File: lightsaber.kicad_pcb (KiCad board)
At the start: 2 copper layers, 31 x 112.5 mm, 8 parts, among them SW1 Button, SW3 POWER, U1 C3 Pico

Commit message: Update PCB for Lightsaber
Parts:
- removed SW3: POWER, as12ap:as12ap
- added SW2: POWER, Button_Switch_SMD:SW_SPDT_CK_JS102011SAQN, B.Cu at (110.7, 59.9)
- added TP1: TO-BAT, TestPoint:TestPoint_Loop_D2.50mm_Drill1.0mm, F.Cu at (113.1, 48.6)
- R1, R2, SW1: moved to B.Cu
- moved R2 124.6 mm to (106.5, 159.1), turned to 180 degrees
- moved R1 52.6 mm to (114.0, 158.7), turned to 0 degrees
- moved R3 48.1 mm to (111.5, 157.5), turned to 90 degrees
- moved BT1 36.3 mm to (120.8, 57.9)
- moved U1 33.9 mm to (120.5, 147.5)
- moved NP1 24.8 mm to (120.5, 39.0)
- moved SW1 22.2 mm to (128.9, 56.0), turned to -90 degrees
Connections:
- BT1 pad 1: +4V -> VBAT
- U1 pad 15: +4V -> unconnected-(U1-IO3/VBAT-Pad15)
- U1 pad 16: Power -> unconnected-(U1-RST/EN-Pad16)
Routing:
- net GND: track 112.6 -> 0.00 mm, vias 4 -> 0
- net +3V3: track 110.2 -> 2.65 mm
- net +4V: track 115.4 -> 24.5 mm
- net Poti: track 103.5 -> 12.8 mm
- net Light: track 33.8 -> 6.13 mm
- net Power: track 23.0 -> 0.00 mm
- net Button: track 84.8 -> 100.0 mm
- net Neopixel: track 101.9 -> 116.5 mm
- net VBAT: track 0.00 -> 8.12 mm
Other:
- board size 31 x 112.5 mm -> 31.5 x 126 mm

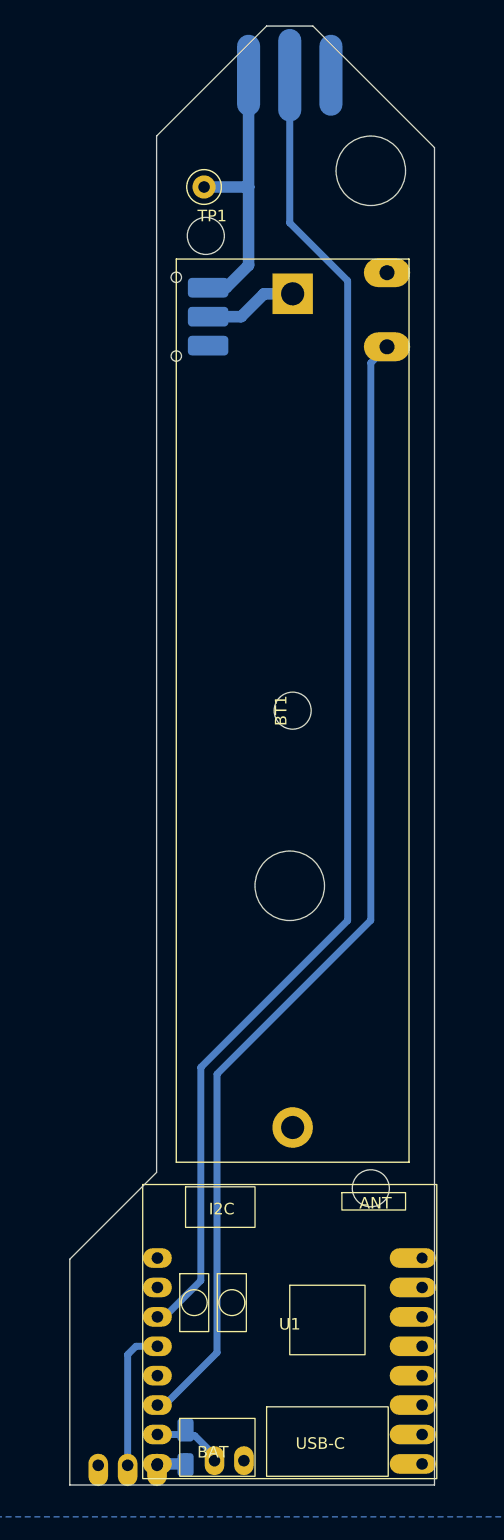
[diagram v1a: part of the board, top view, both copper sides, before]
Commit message: Fixed switch between 5V and V_Batt
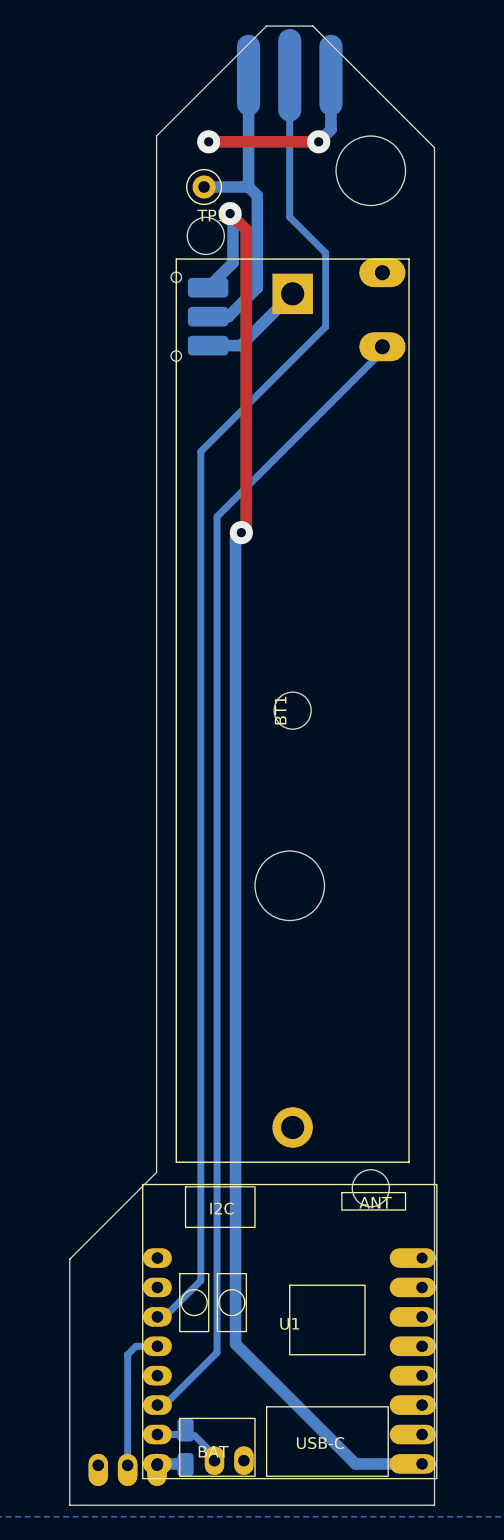
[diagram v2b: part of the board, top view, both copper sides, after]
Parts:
- R3: value R -> 100k
- moved SW1 0.40 mm to (128.5, 56.0)
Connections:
- SW2 pad 1: unconnected-(SW2-A-Pad1) -> VBAT
- SW2 pad 2: VBAT -> +4V
- SW2 pad 3: +4V -> +5V
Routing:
- net +5V: track 0.00 -> 126.4 mm, vias 0 -> 2
- net GND: track 0.00 -> 15.7 mm, vias 0 -> 2
- net +4V: track 24.5 -> 27.8 mm
- net Neopixel: track 116.5 -> 114.9 mm
- net VBAT: track 8.12 -> 9.15 mm
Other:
- board size 31.5 x 126 mm -> 31.5 x 127.8 mm
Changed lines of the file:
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@@
 		(pad_to_mask_clearance 0)
 		(allow_soldermask_bridges_in_footprints no)
-		(grid_origin 120.5 39)
+		(grid_origin 120.5 35)
 		(pcbplotparams
 			(layerselection 0x0001000_fffffffe)
@@
 	(net 17 "unconnected-(U1-IO3{slash}VBAT-Pad15)")
 	(net 18 "VBAT")
-	(net 19 "unconnected-(SW2-A-Pad1)")
 	(footprint "c3-pico:c3-pico"
 		(layer "F.Cu")
@@
 		(model "${KIPRJMOD}/lib/c3-pico/c3-pico.step"
 			(offset
+				(xyz 0 0 2.54)
+			)
+			(scale
+				(xyz 1 1 1)
+			)
+			(rotate
 				(xyz 0 0 0)
+			)
+		)
+		(model "${KICAD_3DMODEL_DIR}/Connector_PinHeader_2.54mm.3dshapes/PinHeader_1x08_P2.54mm_Vertical.wrl"
+			(offset
+				(xyz -11.5 6.5 0)
+			)
+			(scale
+				(xyz 1 1 1)
+			)
+			(rotate
+				(xyz 0 0 0)
+			)
+		)
+		(model "${KICAD_3DMODEL_DIR}/Connector_PinHeader_2.54mm.3dshapes/PinHeader_1x08_P2.54mm_Vertical.wrl"
+			(offset
+				(xyz 11.5 6.5 0)
 			)
 			(scale
@@
 			)
 		)
-		(property "Value" "R"
+		(property "Value" "100k"
 			(at 0 -1.65 90)
 			(layer "B.Fab")
@@
 			(layers "B.Cu" "B.Paste" "B.Mask")
 			(roundrect_rratio 0.2)
-			(net 19 "unconnected-(SW2-A-Pad1)")
+			(net 18 "VBAT")
 			(pinfunction "A")
-			(pintype "passive+no_connect")
+			(pintype "passive")
 		)
 		(pad "2" smd roundrect
@@
 			(layers "B.Cu" "B.Paste" "B.Mask")
 			(roundrect_rratio 0.2)
-			(net 18 "VBAT")
+			(net 3 "+4V")
 			(pinfunction "B")
 			(pintype "passive")
@@
 			(layers "B.Cu" "B.Paste" "B.Mask")
 			(roundrect_rratio 0.2)
-			(net 3 "+4V")
+			(net 13 "+5V")
 			(pinfunction "C")
 			(pintype "passive")
@@
 	(footprint "pts636:pts636"
 		(layer "B.Cu")
-		(at 128.9 56.05 -90)
+		(at 128.5 56.05 -90)
 		(descr "<b>PTS636 SM43 LFS-1</b><br>")
 		(property "Reference" "SW1"
@@
 	(gr_poly
 		(pts
-			(xy 133 160.75) (xy 101.5 160.75) (xy 101.5 141.25) (xy 109 133.75) (xy 109 44.25) (xy 118.5 34.75)
+			(xy 133 162.5) (xy 101.5 162.5) (xy 101.5 141.25) (xy 109 133.75) (xy 109 44.25) (xy 118.5 34.75)
 			(xy 122.5 34.75) (xy 133 45.25)
 		)
@@
 	)
 	(segment
-		(start 113.45 57.35)
-		(end 115 57.35)
+		(start 123 44.75)
+		(end 113.5 44.75)
+		(width 1)
+		(layer "F.Cu")
+		(net 1)
+	)
+	(via
+		(at 113.5 44.75)
+		(size 2)
+		(drill 0.8)
+		(layers "F.Cu" "B.Cu")
+		(net 1)
+	)
+	(via
+		(at 123 44.75)
+		(size 2)
+		(drill 0.8)
+		(layers "F.Cu" "B.Cu")
+		(net 1)
+	)
+	(segment
+		(start 124.056 43.694)
+		(end 123 44.75)
+		(width 1)
+		(layer "B.Cu")
+		(net 1)
+	)
+	(segment
+		(start 124.056 39)
+		(end 124.056 43.694)
+		(width 1)
+		(layer "B.Cu")
+		(net 1)
+	)
+	(segment
+		(start 113.45 59.85)
+		(end 115.2 59.85)
 		(width 1)
 		(layer "B.Cu")
@@
 	)
 	(segment
-		(start 116.944 55.406)
+		(start 115.2 59.85)
+		(end 117.7 57.35)
+		(width 1)
+		(layer "B.Cu")
+		(net 3)
+	)
+	(segment
+		(start 117.7 49.406)
 		(end 116.944 48.65)
 		(width 1)
@@
 	)
 	(segment
-		(start 115 57.35)
-		(end 116.944 55.406)
+		(start 117.7 57.35)
+		(end 117.7 49.406)
 		(width 1)
 		(layer "B.Cu")
@@
 	)
 	(segment
-		(start 125.5 56.75)
-		(end 120.5 51.75)
-		(width 0.6)
-		(layer "B.Cu")
-		(net 5)
-	)
-	(segment
-		(start 120.5 51.75)
-		(end 120.5 39)
-		(width 0.6)
-		(layer "B.Cu")
-		(net 5)
-	)
-	(segment
-		(start 125.5 112)
-		(end 125.5 56.75)
-		(width 0.6)
-		(layer "B.Cu")
-		(net 5)
-	)
-	(segment
-		(start 112.82 143.097716)
-		(end 112.82 124.68)
-		(width 0.6)
-		(layer "B.Cu")
-		(net 5)
-	)
-	(segment
 		(start 109.687716 146.23)
 		(end 112.82 143.097716)
@@
 	)
 	(segment
+		(start 123.6 54.35)
+		(end 120.5 51.25)
+		(width 0.6)
+		(layer "B.Cu")
+		(net 5)
+	)
+	(segment
 		(start 109.07 146.23)
 		(end 109.687716 146.23)
@@
 	)
 	(segment
-		(start 112.82 124.68)
-		(end 125.5 112)
+		(start 112.82 143.097716)
+		(end 112.82 71.505)
+		(width 0.6)
+		(layer "B.Cu")
+		(net 5)
+	)
+	(segment
+		(start 123.6 60.725)
+		(end 123.6 54.35)
+		(width 0.6)
+		(layer "B.Cu")
+		(net 5)
+	)
+	(segment
+		(start 120.5 51.25)
+		(end 120.5 39)
+		(width 0.6)
+		(layer "B.Cu")
+		(net 5)
+	)
+	(segment
+		(start 112.82 71.505)
+		(end 123.6 60.725)
 		(width 0.6)
 		(layer "B.Cu")
@@
 	)
 	(segment
-		(start 127.5 111.979898)
-		(end 127.5 63.85)
-		(width 0.6)
-		(layer "B.Cu")
-		(net 15)
-	)
-	(segment
-		(start 114.22 149.317716)
-		(end 114.22 125.259898)
-		(width 0.6)
-		(layer "B.Cu")
-		(net 15)
+		(start 116.75 52.348365)
+		(end 115.351635 50.95)
+		(width 1)
+		(layer "F.Cu")
+		(net 13)
+	)
+	(segment
+		(start 116.75 78.07)
+		(end 116.75 52.348365)
+		(width 1)
+		(layer "F.Cu")
+		(net 13)
+	)
+	(segment
+		(start 116.32 78.5)
+		(end 116.75 78.07)
+		(width 1)
+		(layer "F.Cu")
+		(net 13)
+	)
+	(via
+		(at 116.32 78.5)
+		(size 2)
+		(drill 0.8)
+		(layers "F.Cu" "B.Cu")
+		(net 13)
+	)
+	(via
+		(at 115.351635 50.95)
+		(size 2)
+		(drill 0.8)
+		(layers "F.Cu" "B.Cu")
+		(net 13)
+	)
+	(segment
+		(start 126.18 158.93)
+		(end 131.93 158.93)
+		(width 1)
+		(layer "B.Cu")
+		(net 13)
+	)
+	(segment
+		(start 116.32 78.5)
+		(end 115.82 79)
+		(width 1)
+		(layer "B.Cu")
+		(net 13)
+	)
+	(segment
+		(start 115.82 79)
+		(end 115.82 148.57)
+		(width 1)
+		(layer "B.Cu")
+		(net 13)
+	)
+	(segment
+		(start 115.6 51.198365)
+		(end 115.351635 50.95)
+		(width 1)
+		(layer "B.Cu")
+		(net 13)
+	)
+	(segment
+		(start 115.6 55.2)
+		(end 115.6 51.198365)
+		(width 1)
+		(layer "B.Cu")
+		(net 13)
+	)
+	(segment
+		(start 115.82 148.57)
+		(end 126.18 158.93)
+		(width 1)
+		(layer "B.Cu")
+		(net 13)
+	)
+	(segment
+		(start 113.45 57.35)
+		(end 115.6 55.2)
+		(width 1)
+		(layer "B.Cu")
+		(net 13)
 	)
 	(segment
@@
 	)
 	(segment
-		(start 127.5 63.85)
-		(end 128.9 62.45)
-		(width 0.6)
-		(layer "B.Cu")
-		(net 15)
-	)
-	(segment
 		(start 109.07 153.85)
 		(end 109.687716 153.85)
@@
 	)
 	(segment
-		(start 114.22 125.259898)
-		(end 127.5 111.979898)
+		(start 128.5 62.85)
+		(end 128.5 62.45)
 		(width 0.6)
 		(layer "B.Cu")
@@
 	)
 	(segment
-		(start 118.275 57.875)
-		(end 116.3 59.85)
+		(start 114.22 149.317716)
+		(end 114.22 77.13)
+		(width 0.6)
+		(layer "B.Cu")
+		(net 15)
+	)
+	(segment
+		(start 114.22 77.13)
+		(end 128.5 62.85)
+		(width 0.6)
+		(layer "B.Cu")
+		(net 15)
+	)
+	(segment
+		(start 113.45 62.35)
+		(end 116.275 62.35)
 		(width 1)
 		(layer "B.Cu")
@@
 	)
 	(segment
-		(start 120.75 57.875)
-		(end 118.275 57.875)
+		(start 116.275 62.35)
+		(end 120.75 57.875)
 		(width 1)
 		(layer "B.Cu")
-		(net 18)
-	)
-	(segment
-		(start 116.3 59.85)
-		(end 113.45 59.85)
-		(width 1)
-		(layer "B.Cu")
